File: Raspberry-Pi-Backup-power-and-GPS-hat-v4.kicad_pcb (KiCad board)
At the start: 2 copper layers, 160 x 90 mm, 60 parts, among them J1 GPIO, J3 Conn_01x02_Pin, J4 Conn_01x02_Pin, U1 ESP32-DEVKIT-V1, U10 B0505S-1WR3, U11 TC2185-3.3VxCTTR, U12 LAN8651B1-E/LMX, U3 MCP2515-xSO, U6 MCP2515-xSO, U7 SN65HVD230, U8 SN65HVD230, U9 Si8642ED-B-IS, Y1 8MHz, Y2 8MHz, Y3 25MHz

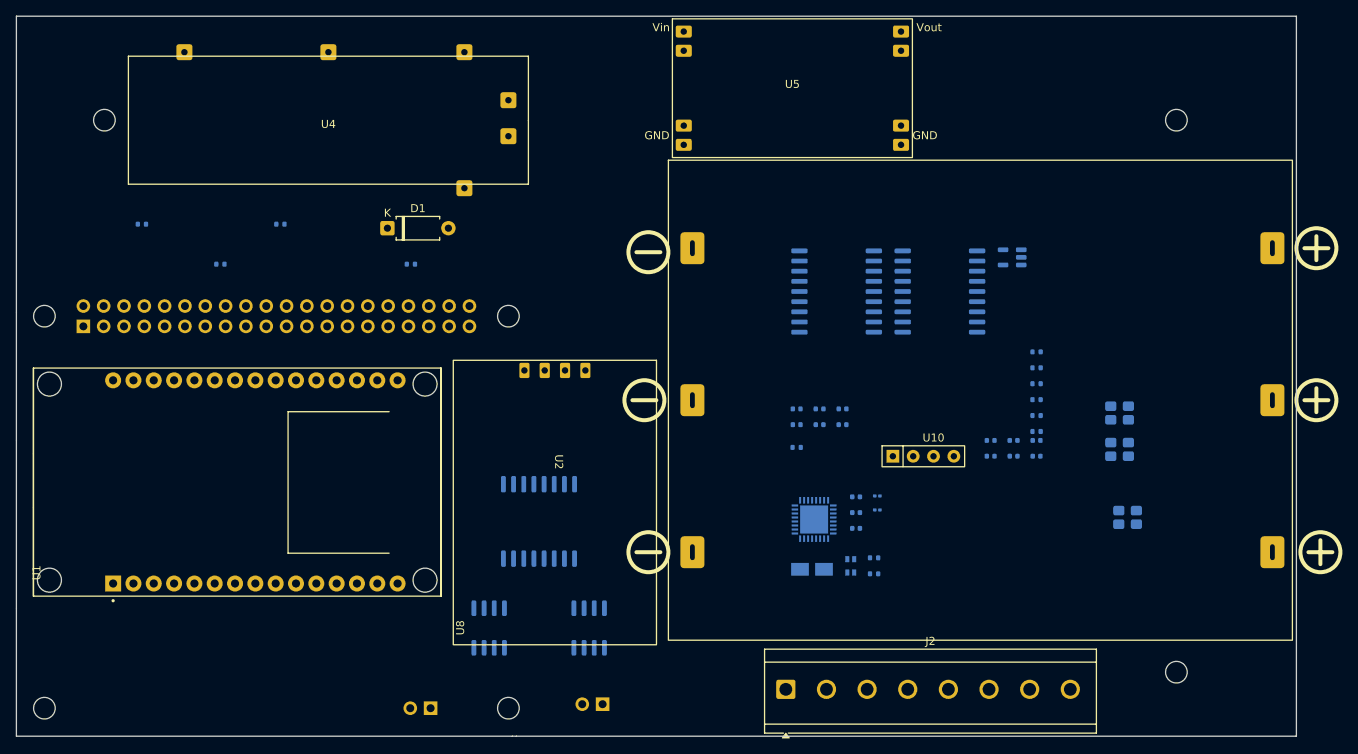
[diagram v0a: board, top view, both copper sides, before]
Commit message: Remove non-existent security fields from bluer characteristics
The bluer crate's CharacteristicWrite and CharacteristicNotify
don't have encrypt_*/secure_* fields - removed them.

Co-Authored-By: Claude Opus 4.5 <noreply@anthropic.com>
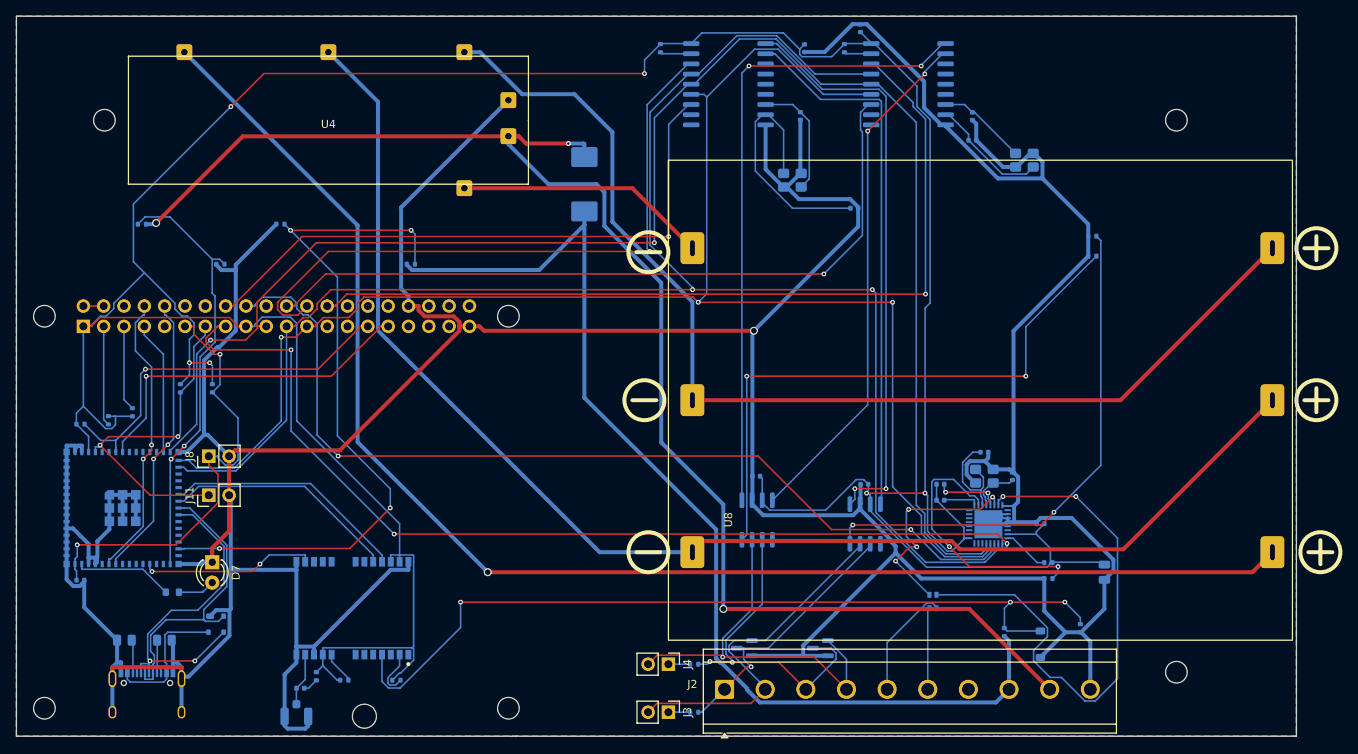
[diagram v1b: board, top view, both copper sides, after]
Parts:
- removed C3, C6: 10uF, Capacitor_SMD:C_0402_1005Metric
- removed C4: 1uF, Capacitor_SMD:C_0402_1005Metric
- removed C5: 100nF, Capacitor_SMD:C_0402_1005Metric
- removed R9: 1k, Resistor_SMD:R_0402_1005Metric
- removed U10: B0505S-1WR3, Resistor_THT:R_Array_SIP4
- removed U11: TC2185-3.3VxCTTR, Package_TO_SOT_SMD:SOT-23-5
- removed U5: ~, Perfect Precision:MP4560
- removed U9: Si8642ED-B-IS, Package_SO:SOIC-16W_7.5x10.3mm_P1.27mm
- added C17: 1uF, Capacitor_SMD:C_0402_1005Metric, B.Cu at (108.0, 170.5)
- added D2: D_TVS_Dual_ACA, Package_TO_SOT_SMD:SOT-23, B.Cu at (191.0, 179.0)
- added D3: D_TVS_Dual_ACA, Package_TO_SOT_SMD:SOT-23, B.Cu at (200.5, 179.0)
- added D4: PRTR5V0U2X, Package_TO_SOT_SMD:SOT-143, B.Cu at (125.0, 176.0)
- added D5: 3.3v, Diode_SMD:D_SOD-123, B.Cu at (228.0, 178.5)
- added D7: LED, LED_THT:LED_D3.0mm, F.Cu at (124.5, 168.3)
- added J11: Boot, Connector_PinHeader_2.54mm:PinHeader_1x02_P2.54mm_Vertical, F.Cu at (124.0, 159.9)
- added J5: USB_C_Receptacle_USB2.0_16P, Connector_USB:USB_C_Receptacle_HRO_TYPE-C-31-M-12, B.Cu at (116.3, 185.9)
- added J6: Conn_Coaxial, Connector_Coaxial:U.FL_Hirose_U.FL-R-SMT-1_Vertical, B.Cu at (135.0, 187.1)
- added J8: Reset, Connector_PinHeader_2.54mm:PinHeader_1x02_P2.54mm_Vertical, F.Cu at (124.0, 155.0)
- added L2: 47nH, Inductor_SMD:L_0402_1005Metric, B.Cu at (135.5, 184.0)
- added R14: 10k, Resistor_SMD:R_0402_1005Metric, B.Cu at (120.5, 146.5)
- added R15: 10k, Resistor_SMD:R_0402_1005Metric, B.Cu at (124.5, 146.5)
- added R16: 10k, Resistor_SMD:R_0402_1005Metric, B.Cu at (223.5, 177.0)
- added R17: 100k, Resistor_SMD:R_0402_1005Metric, B.Cu at (233.0, 176.5)
- added R18: 10k, Resistor_SMD:R_0402_1005Metric, B.Cu at (147.5, 183.0)
- added R19: 10k, Resistor_SMD:R_0402_1005Metric, B.Cu at (141.0, 183.0)
- added R20: 200R, Resistor_SMD:R_0603_1608Metric, B.Cu at (119.5, 172.0)
- added R21: 4k7, Resistor_SMD:R_0402_1005Metric, B.Cu at (114.5, 149.5)
- added R22: 4k7, Resistor_SMD:R_0402_1005Metric, B.Cu at (111.5, 150.5)
- added R23: 10k, Resistor_SMD:R_0402_1005Metric, B.Cu at (108.0, 151.0)
- added R24: 10R, Resistor_SMD:R_0402_1005Metric, B.Cu at (137.5, 182.5)
- added R34: 5k1, Resistor_SMD:R_0805_2012Metric, B.Cu at (118.5, 178.0)
- added R35: 5k1, Resistor_SMD:R_0805_2012Metric, B.Cu at (113.5, 178.0)
- C16: footprint Capacitor_SMD:CP_Elec_3x5.3 -> Capacitor_SMD:C_0805_2012Metric
- C2: value 22nF -> 100nF
- D1: footprint Diode_THT:D_A-405_P7.62mm_Horizontal -> Diode_SMD:D_SMC; moved to B.Cu
- FB1, FB2: footprint Inductor_SMD:L_0201_0603Metric -> Inductor_SMD:L_0402_1005Metric
- J2: footprint TerminalBlock_CUI:TerminalBlock_CUI_TB007-508-08_1x08_P5.08mm_Horizontal -> TerminalBlock_CUI:TerminalBlock_CUI_TB007-508-10_1x10_P5.08mm_Horizontal
- J3, J4: moved to F.Cu
- R1, R4: value 400k -> 470k
- U1: value ESP32-DEVKIT-V1 -> NEO-M9N-00B; footprint ESP32-DEVKIT-V1:MODULE_ESP32_DEVKIT_V1 -> Perfect Precision:SMT_9N-00B_UBL; moved to B.Cu
- U2: value ~ -> ESP32-S3-MINI-1; footprint NEO M6 Board:NEO M6 GPS Board -> RF_Module:ESP32-S2-MINI-1; moved to B.Cu
- moved R5 60.4 mm to (180.5, 104.0), turned to 90 degrees
- moved C12 57.9 mm to (205.5, 101.5), turned to -90 degrees
- moved C11 57.0 mm to (198.5, 104.0), turned to 90 degrees
- moved U2 56.9 mm to (110.7, 161.5)
- moved R10 55.3 mm to (184.7, 187.0), turned to 0 degrees
- moved Y1 50.2 mm to (197.0, 120.5)
- moved R6 46.6 mm to (203.5, 104.0), turned to 90 degrees
- moved C7 40.9 mm to (219.5, 112.5), turned to 90 degrees
- moved C8 39.8 mm to (219.5, 115.5)
- moved Y2 38.1 mm to (226.0, 118.0), turned to 0 degrees
- moved U7 36.9 mm to (206.1, 163.5)
- moved C9 36.6 mm to (198.0, 112.5), turned to 90 degrees
- moved C16 36.6 mm to (236.0, 169.5), turned to -90 degrees
- moved U8 36.1 mm to (192.6, 163.0)
- moved J4 30.2 mm to (181.5, 181.0), turned to -90 degrees
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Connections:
- net /Power renamed V_TRACTOR
- C1 pad 1: +3.3VS -> +3.3V
- C1 pad 2: SGND -> GND
- C2 pad 1: Net-(U11-BP) -> +3.3V
- C2 pad 2: SGND -> GND
- J1 pad 1: +3V3 -> +3.3V
- J1 pad 10: /GPIO15/RXD0 -> RXD0
- J1 pad 11: /GPIO17 -> GPIO17
- J1 pad 13: /GPIO27 -> GPIO27
- J1 pad 17: +3V3 -> +3.3V
- J1 pad 29: /GPIO5 -> GPIO5
- J1 pad 3: /GPIO2/SDA1 -> SDA1
- J1 pad 31: /GPIO6 -> GPIO6
- J1 pad 5: /GPIO3/SCL1 -> SCL1
- J1 pad 7: /GPIO4/GPCLK0 -> GPIO4_CS
- J1 pad 8: /GPIO14/TXD0 -> TXD0
- R1 pad 2: /DATA -> D34
- R2 pad 1: /DATA -> D34
- R3 pad 1: Net-(U1-D35) -> D35
- R4 pad 2: Net-(U1-D35) -> D35
- R7 pad 2: SGND -> GND
- R8 pad 2: SGND -> GND
- U1 pad 10: unconnected-(U1-D19-Pad10) -> GND
- U1 pad 11: /GPIO2/SDA1 -> Net-(J6-In)
- U1 pad 12: unconnected-(U1-RX0-Pad12) -> GND
- U1 pad 13: unconnected-(U1-TX0-Pad13) -> GND
- U1 pad 14: /GPIO3/SCL1 -> LNA_EN
- U1 pad 19: /DATA -> unconnected-(U1-SCL_/_SPI_SLK-Pad19)
- U1 pad 2: GND -> Net-(U1-D_SEL)
- U1 pad 20: Net-(U1-D35) -> RXD1
- U1 pad 21: unconnected-(U1-D32-Pad21) -> TXD1
- U1 pad 22: unconnected-(U1-D33-Pad22) -> +3.3V
- U1 pad 23: unconnected-(U1-D25-Pad23) -> +3.3V
- U1 pad 24: unconnected-(U1-D26-Pad24) -> GND
- U1 pad 4: /GPIO17 -> Net-(D5-K)
- U1 pad 5: /GPIO27 -> unconnected-(U1-USB_DM-Pad5)
- U1 pad 8: unconnected-(U1-D5-Pad8) -> Net-(U1-RESET_N)
- U1 pad 9: unconnected-(U1-D18-Pad9) -> +3.3V
- U2 pad 1: /3v3 -> GND
- U2 pad 2: /GPIO14/TXD0 -> GND
- U2 pad 3: /GPIO15/RXD0 -> +3.3V
- U2 pad 4: GND -> GPIO27
- U7 pad 1: Net-(U7-D) -> Net-(U3-TXCAN)
- U7 pad 2: SGND -> GND
- U7 pad 3: +3.3VS -> +3.3V
- U7 pad 4: Net-(U7-R) -> Net-(U3-RXCAN)
- U8 pad 1: Net-(U8-D) -> Net-(U6-TXCAN)
- U8 pad 2: SGND -> GND
- U8 pad 3: +3.3VS -> +3.3V
- U8 pad 4: Net-(U8-R) -> Net-(U6-RXCAN)
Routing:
- net GND: track 0.00 -> 662.6 mm, vias 0 -> 1
- net +3.3V: track 0.00 -> 429.6 mm, vias 0 -> 6
- net MISO: track 0.00 -> 208.9 mm, vias 0 -> 2
- net SCK: track 0.00 -> 200.2 mm, vias 0 -> 3
- net MOSI: track 0.00 -> 197.9 mm, vias 0 -> 2
- net /Power Li+: track 0.00 -> 181.4 mm, vias 0 -> 3
- net /Power B3: track 0.00 -> 179.8 mm, vias 0 -> 1
- net /Power B2: track 0.00 -> 169.4 mm
- net /Power B1: track 0.00 -> 140.7 mm
- net V_TRACTOR: track 0.00 -> 134.1 mm
- net GPIO22: track 0.00 -> 121.8 mm, vias 0 -> 3
- net GPIO24: track 0.00 -> 117.4 mm, vias 0 -> 2
- net CE1: track 0.00 -> 107.3 mm, vias 0 -> 1
- net Net-(D5-K): track 0.00 -> 107.1 mm, vias 0 -> 3
- net GPIO25: track 0.00 -> 93.0 mm, vias 0 -> 1
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- added copper zone on B.Cu, net GND
- added copper zone on F.Cu, net GND
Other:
- outline, holes or cut-outs redrawn
